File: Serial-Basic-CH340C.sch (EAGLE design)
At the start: 23 parts, among them U1 AP2112-3.3V, U5 CH340C

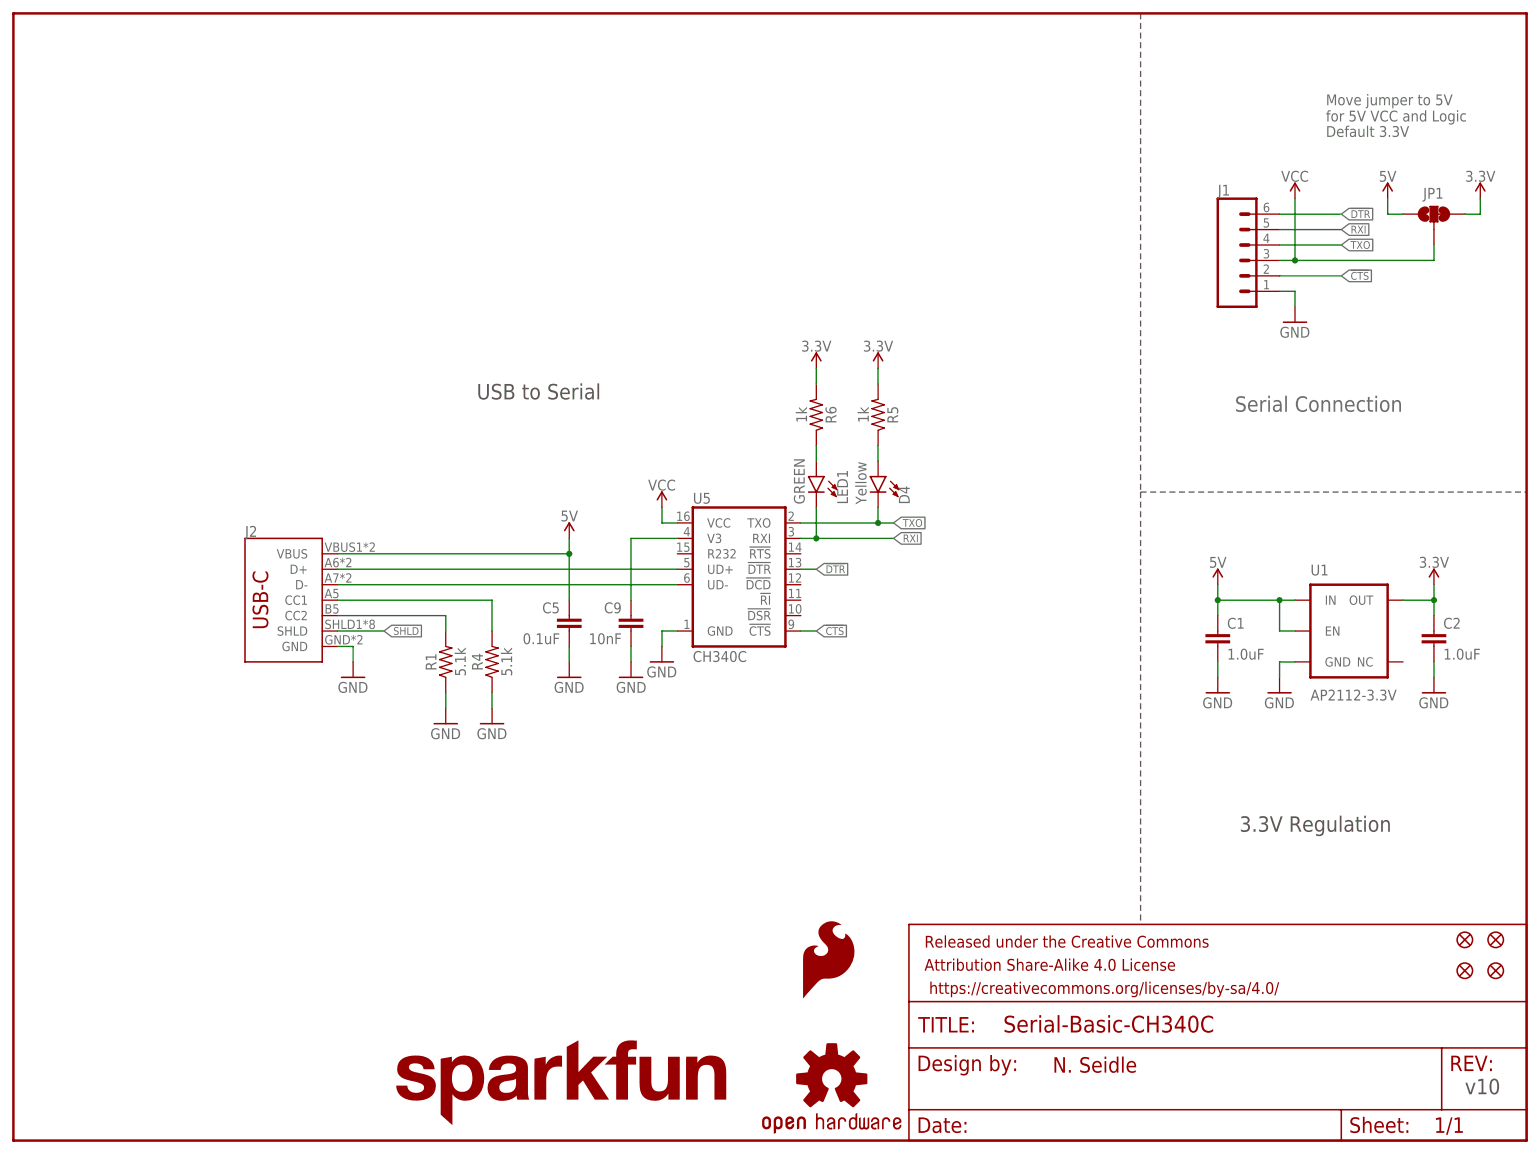
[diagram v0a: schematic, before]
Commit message: Updating libraries, tidied up schematic, deleted unneccessary files, adding readme outline
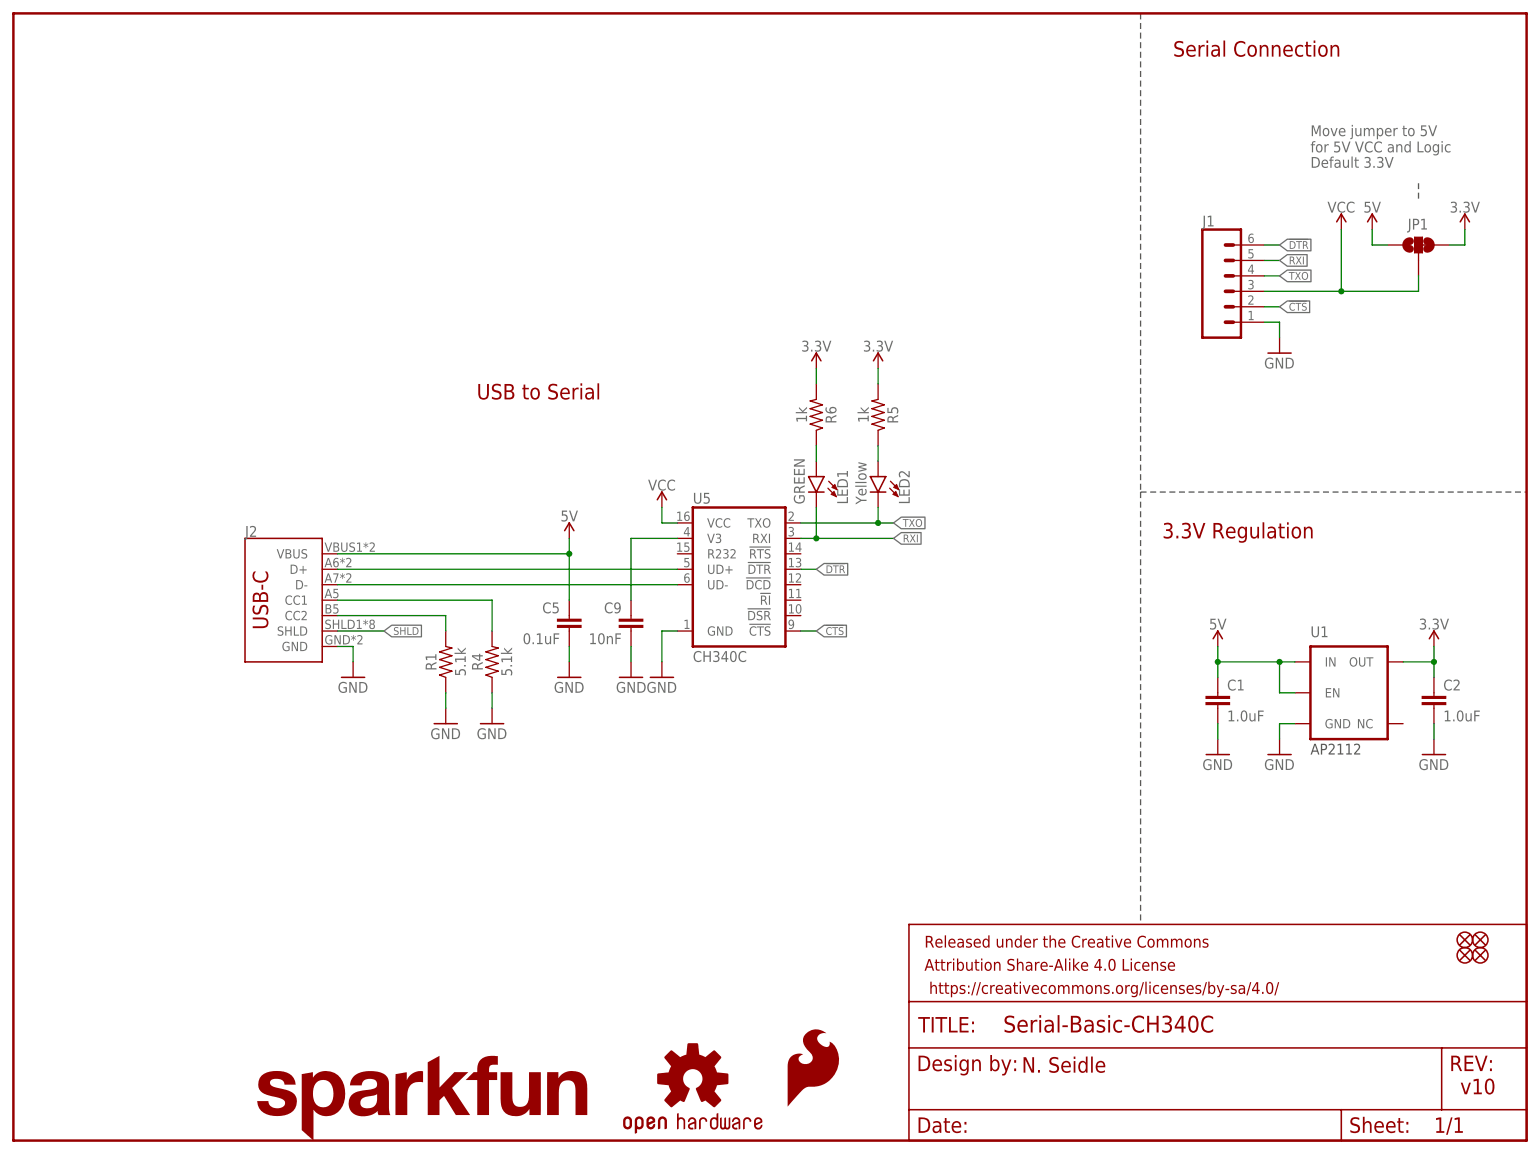
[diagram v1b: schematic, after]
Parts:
- J2: device USB-C:USB_C16PIN -> SparkFun-Connectors:USB_C16PIN
- U1: value AP2112-3.3V -> 3.3V; device SparkFun-PowerIC:V_REG_AP2112K-3.3V -> SparkFun-IC-Power:V_REG_AP2112K-3.3V
- renumbered D4 to LED2
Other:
- note added: "AP2112"
- moved on the sheet: C1, C2, J1, JP1, U1
